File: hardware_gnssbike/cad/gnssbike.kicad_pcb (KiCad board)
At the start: 4 copper layers, 50 x 86 mm, 113 parts, among them J101 Molex 2036150003, J102 JST SM06B-GHS-TB, J201 Tag-Connect TC2030-NL, J401 Hirose FH28-10S-0.5SH, J402 Molex 503480-0500, Q401 DMG1012T-7, Q601 DMG1012T-7, Q602 DMG1012T-7, Q603 DMG1012T-7, SW601 Omron B3S-1002P, SW602 Omron B3S-1002P, SW603 Omron B3S-1002P, U101 nPM1300-QEAA, U102 MAX17262REWL, U103 AEM10900, U104 TPS7A0218PDQN, U201 MinewSemi ME54BS13, U301 u-blox MAX-F10S, U302 TI TXU0204BQAR, U501 MX25R6435F, U502 Bosch BMP585, U503 Bosch BMI270, U504 MMC5633NJL, U505 TI OPT3001DNPR

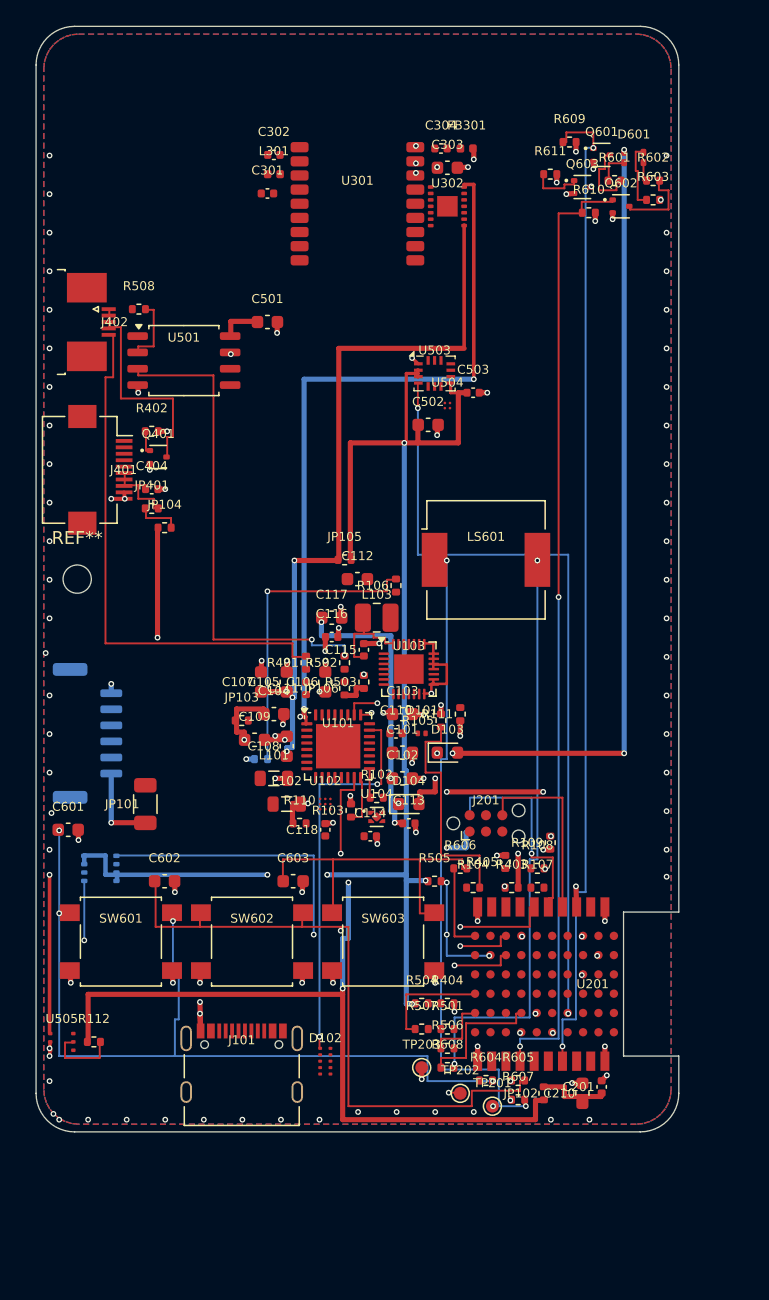
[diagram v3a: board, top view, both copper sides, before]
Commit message: fix(hardware): 45 degree corners, a 50 ohm line, and the stack-up that allows it
Three things the owner was right to call out, and one of them ran deeper than
it looked.

The router could only move four ways, so EVERY corner it drew was a right
angle. It now moves eight, with the guard that a diagonal step may not cut a
corner: both orthogonal cells it passes between have to be free too. Of 755
segments, 331 are now diagonal.

The RF line was left unrouted with the excuse that the 50 ohm width "does not
exist yet". It does: the stack-up is in the board file. Solving Hammerstad's
microstrip formula for 50 ohm on the dielectric that was there, 0.22 mm, gives
0.431 mm of track - and that is why the excuse held, because 0.431 mm cannot
leave the receiver's pin between pads on a 1.1 mm pitch.

The answer was not to give up but to read the sentence after the requirement.
Section 4.4 of the MAX-F10S integration manual says to "select the stack-up,
copper, and dielectric properties of the PCB accordingly to fulfil this
condition". The stack-up serves the RF line, not the other way round. It is
now asymmetric - 0.10 mm of prepreg to the ground plane, a 0.46 mm core,
0.10 mm back - which is the usual four layer arrangement for a board with RF
and brings 50 ohm to 0.196 mm. RF_ANT routes at that width.

And the rule this file had added itself - no signal under the GNSS receiver,
from the same section 4.4 - was blocking the receiver's own RF line, which
lives under the receiver by definition. "Signal lines crossing below" means
somebody else's. The RF nets now route first and the area closes behind them.

Five manufacturer datasheets were read for their layout sections, and two of
their rules are measurable and are now measured:

  TPS7A02 SBVS277C 8.4.1: no thermal via directly beneath the thermal pad of
  a DQN package - it wicks solder away from the joint;
  OPT3001: no component closer than twice its own height to the light
  sensor, because of secondary optical reflections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
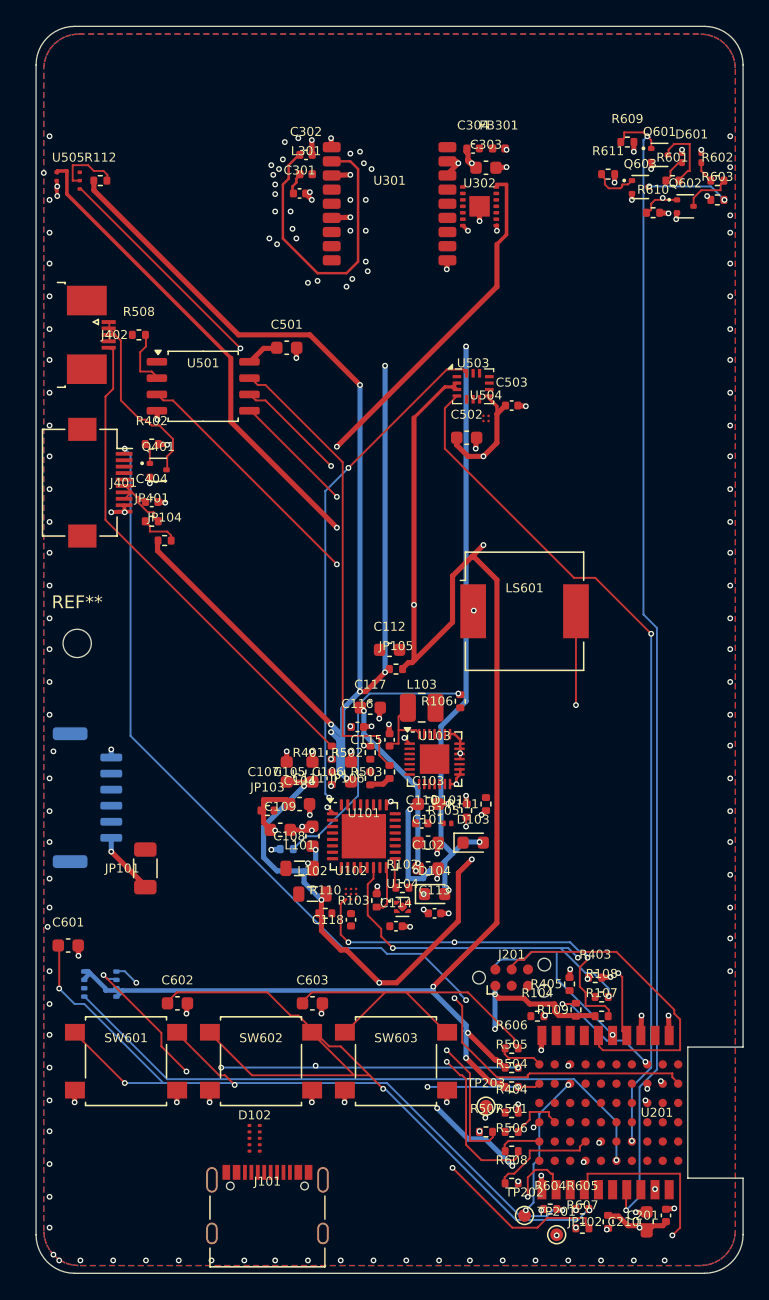
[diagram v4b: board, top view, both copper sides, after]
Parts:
- moved R112 67.0 mm to (30.0, 37.0)
- moved U505 67.0 mm to (27.5, 37.0)
- moved R505 15.7 mm to (62.0, 106.0)
- moved R606 14.6 mm to (62.0, 104.5)
- moved R109 13.2 mm to (67.0, 101.5)
- moved J201 12.2 mm to (62.0, 99.0)
- moved C201 11.2 mm to (74.0, 117.5)
- moved C210 11.2 mm to (72.5, 118.0)
- moved JP102 11.2 mm to (69.5, 118.0)
- moved R104 11.2 mm to (64.0, 102.0)
- moved R107 11.2 mm to (69.0, 102.0)
- moved R108 11.2 mm to (69.0, 100.5)
- moved R604 11.2 mm to (65.0, 117.0)
- moved R605 11.2 mm to (67.5, 117.0)
- moved R607 11.2 mm to (67.5, 118.5)
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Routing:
- net SENS_SDA: track 0.00 -> 101.1 mm, vias 0 -> 6
- net DISP_SCK: track 0.00 -> 77.4 mm, vias 0 -> 3
- net GNSS_RESET_N: track 71.4 -> 0.00 mm, vias 2 -> 0
- net NOR_SCK_F: track 0.00 -> 71.0 mm, vias 0 -> 2
- net SENS_SCL: track 41.8 -> 110.3 mm, vias 4 -> 5
- net NOR_MOSI_F: track 0.00 -> 67.9 mm, vias 0 -> 2
- net PWR_SDA: track 0.00 -> 56.3 mm, vias 0 -> 4
- net 3V0_SENS: track 134.9 -> 178.5 mm, vias 6 -> 7
- net 3V0: track 203.8 -> 242.1 mm, vias 14 -> 20
- net CC1: track 30.5 -> 0.00 mm, vias 2 -> 0
- net PWR_SCL: track 11.1 -> 40.8 mm, vias 2 -> 4
- net RF_IN: track 0.00 -> 24.0 mm
- net RGB_G: track 74.2 -> 97.7 mm
- net RGB_R: track 77.8 -> 90.6 mm
- net LED_CHG: track 11.2 -> 0.00 mm, vias 2 -> 0
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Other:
- board size 50 x 86 mm -> 55 x 97 mm

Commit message: feat(hardware): the AEM10900's own layout rules, and two real heights
The energy harvester's datasheet has a layout section and this board was not
following it. Section 13 of DS-AEM1090x-v2.4.0, word for word: "PCB track
capacitance must be reduced as much as possible on the boost converter
switching node SWDCDC. This is done as follows: keep the connection between
the SWDCDC pin and the inductor short; REMOVE THE GROUND AND POWER PLANES
UNDER THE SWDCDC NODE - the polygon on the opposite external layer may also
be removed - increase the distance between SWDCDC and the ground polygon on
the external PCB layer where the AEM1090x is mounted." And the same for
TH_REF.

Every pour on this board covered that node. A plane under a switching node is
capacitance the converter charges and discharges at its switching frequency,
and on a harvester that runs on microwatts that is not a detail. The board
now carries a computed keep-out over each of the two nodes - computed,
because it follows wherever the placer puts the part - and it forbids the
POUR, not the track: the node's own copper has to be there, and forbidding it
too put sixteen items_not_allowed in the DRC, every one of them the switching
node itself. The router also keeps its stitching vias out, since a ground via
there brings the plane straight back.

Two heights stopped being guesses. The tactile key is 3.4 mm, not the 5.0 mm
this file assumed, read off the dimensioned drawing on page 2 of the Omron
B3S datasheet - body 6.0 x 6.0, plunger 3.3 mm across standing 0.7 mm proud.
The buzzer is 11.0 x 9.0 x 1.7 mm, from the CPT-1117-83-SMT datasheet, which
is the part on the bill of materials; the 3.0 mm here was for the CPT-9019S
that only the footprint is named after.

Ten more manufacturer datasheets came in from the earlier work in this
session and now sit in datasheets/, which the .gitignore keeps out of this
public repository: the AEM10900, the Omron key, the buzzer, the USB-C
receptacle, the FPC connector, the fla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
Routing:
- net GND: track 52.5 -> 51.9 mm, vias 176 -> 174
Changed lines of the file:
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@@
 	)
 	(zone
+		(net 0)
+		(net_name "")
+		(layers "F.Cu" "In1.Cu" "In2.Cu" "B.Cu")
+		(name "SEM_PLANO_SW_DCDC")
+		(hatch edge 0.5)
+		(connect_pads
+			(clearance 0)
+		)
+		(min_thickness 0.25)
+		(filled_areas_thickness no)
+		(keepout
+			(tracks allowed)
+(pads allowed)
+			(copperpour not_allowed)
+			(footprints allowed)
+		)
+		(fill
+			(thermal_gap 0.5)
+			(thermal_bridge_width 0.5)
+		)
+		(polygon
+			(pts
+				(xy 53.4625 77.4000)
+				(xy 56.6750 77.4000)
+				(xy 56.6750 83.0000)
+				(xy 53.4625 83.0000)
+			)
+		)
+	)
+	(zone
+		(net 0)
+		(net_name "")
+		(layers "F.Cu" "In1.Cu" "In2.Cu" "B.Cu")
+		(name "SEM_PLANO_TH_REF")
+		(hatch edge 0.5)
+		(connect_pads
+			(clearance 0)
+		)
+		(min_thickness 0.25)
+		(filled_areas_thickness no)
+		(keepout
+			(tracks allowed)
+(pads allowed)
+			(copperpour not_allowed)
+			(footprints allowed)
+		)
+		(fill
+			(thermal_gap 0.5)
+			(thermal_bridge_width 0.5)
+		)
+		(polygon
+			(pts
+				(xy 55.2000 77.6100)
+				(xy 58.4000 77.6100)
+				(xy 58.4000 80.4625)
+				(xy 55.2000 80.4625)
+			)
+		)
+	)
+	(zone
 		(net 32)
 		(net_name "GND")
@@
 	)
 	(segment
-		(start 54.0625 80.8000)
-		(end 53.6500 80.3500)
-		(width 0.2)
-		(layer "F.Cu")
-		(net 32)
-	)
-	(segment
 		(start 74.2500 103.5000)
 		(end 74.2000 101.9500)
@@
 	)
 	(segment
+		(start 45.5500 36.5500)
+		(end 44.9500 37.1500)
+		(width 0.196)
+		(layer "F.Cu")
+		(net 68)
+	)
+	(segment
+		(start 44.9500 37.1500)
+		(end 44.9500 38.0500)
+		(width 0.196)
+		(layer "F.Cu")
+		(net 68)
+	)
+	(segment
 		(start 47.9500 35.5000)
 		(end 49.4500 35.5000)
@@
 	(segment
 		(start 44.2000 41.5000)
-		(end 44.2000 37.3000)
+		(end 44.2000 37.1500)
 		(width 0.196)
 		(layer "F.Cu")
@@
 	)
 	(segment
-		(start 44.2000 37.3000)
-		(end 44.6500 36.8500)
+		(start 44.2000 37.1500)
+		(end 44.6500 36.7000)
 		(width 0.196)
 		(layer "F.Cu")
@@
 	)
 	(segment
-		(start 44.6500 36.8500)
+		(start 44.6500 36.7000)
 		(end 44.6500 35.8000)
 		(width 0.196)
@@
 	)
 	(segment
-		(start 45.5500 36.5500)
-		(end 45.2500 36.8500)
-		(width 0.196)
-		(layer "F.Cu")
-		(net 68)
-	)
-	(segment
-		(start 45.2500 36.8500)
-		(end 45.2500 37.1500)
-		(width 0.196)
-		(layer "F.Cu")
-		(net 68)
-	)
-	(segment
-		(start 45.2500 37.1500)
-		(end 44.9500 37.4500)
-		(width 0.196)
-		(layer "F.Cu")
-		(net 68)
-	)
-	(segment
-		(start 44.9500 37.4500)
-		(end 44.9500 38.0500)
-		(width 0.196)
-		(layer "F.Cu")
-		(net 68)
-	)
-	(segment
 		(start 28.4500 37.0000)
 		(end 27.8500 37.0000)
@@
 	(segment
 		(start 57.7000 83.9500)
-		(end 54.7000 80.9500)
-		(width 0.2)
-		(layer "In2.Cu")
-		(net 99)
-	)
-	(segment
-		(start 54.7000 80.9500)
-		(end 52.6000 80.9500)
+		(end 53.8000 80.0500)
 		(width 0.2)
 		(layer "In2.Cu")
@@
 	)
 	(segment
-		(start 52.6000 80.9500)
-		(end 51.7000 80.0500)
-		(width 0.4)
-		(layer "In2.Cu")
-		(net 99)
-	)
-	(segment
-		(start 51.7000 80.0500)
+		(start 53.8000 80.0500)
 		(end 50.5000 80.0500)
 		(width 0.4)
@@
 	)
 	(via
-		(at 53.6500 80.3500)
-		(size 0.45)
-		(drill 0.25)
-		(layers "F.Cu" "B.Cu")
-		(net 32)
-	)
-	(via
 		(at 74.2000 101.9500)
 		(size 0.45)
@@
 	)
 	(via
+		(at 43.9000 36.1000)
+		(size 0.45)
+		(drill 0.25)
+		(layers "F.Cu" "B.Cu")
+		(net 32)
+	)
+	(via
+		(at 43.6000 37.1500)
+		(size 0.45)
+		(drill 0.25)
+		(layers "F.Cu" "B.Cu")
+		(net 32)
+	)
+	(via
+		(at 43.6000 38.0500)
+		(size 0.45)
+		(drill 0.25)
+		(layers "F.Cu" "B.Cu")
+		(net 32)
+	)
+	(via
 		(at 49.4500 34.9000)
 		(size 0.45)
@@
 	)
 	(via
-		(at 43.6000 37.3000)
+		(at 42.8500 37.1500)
 		(size 0.45)
 		(drill 0.25)
@@
 	)
 	(via
-		(at 43.4500 36.5500)
-		(size 0.45)
-		(drill 0.25)
-		(layers "F.Cu" "B.Cu")
-		(net 32)
-	)
-	(via
-		(at 43.9000 36.1000)
-		(size 0.45)
-		(drill 0.25)
-		(layers "F.Cu" "B.Cu")
-		(net 32)
-	)
-	(via
-		(at 43.3000 35.8000)
+		(at 43.1500 36.1000)
 		(size 0.45)
 		(drill 0.25)
@@
 		(size 0.45)
 		(drill 0.25)
-		(layers "F.Cu" "B.Cu")
-		(net 32)
-	)
-	(via
-		(at 46.3000 37.9000)
-		(size 0.45)
-		(drill 0.25)
-		(layers "F.Cu" "B.Cu")
-		(net 32)
-	)
-	(via
-		(at 43.6000 38.0500)
-		(size 0.45)
-		(drill 0.25)

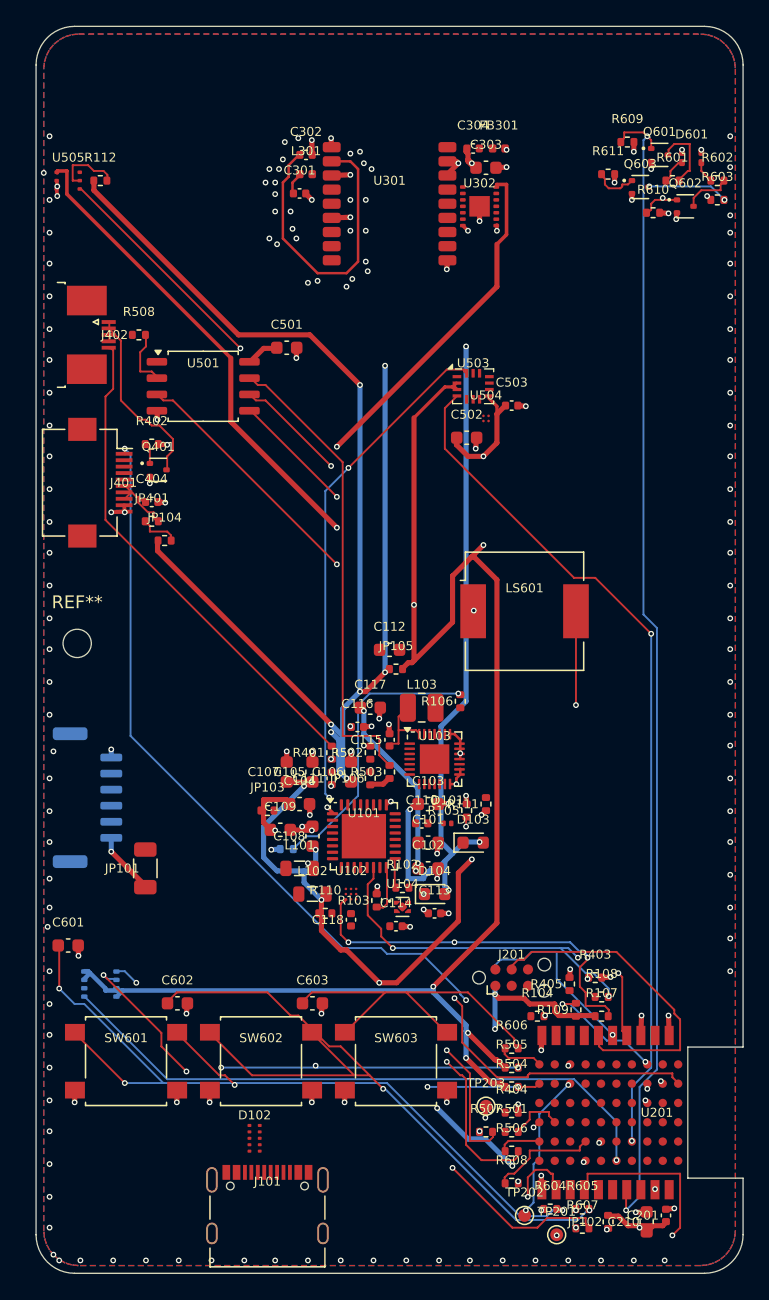
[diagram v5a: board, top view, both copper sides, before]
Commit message: fix(hardware): the solar panel and the antenna had nowhere to touch the board
This board could not be built. The six solar modules live in the case and
connect to SRC and GND; the GNSS antenna element lives in the case wall and
connects to RF_ANT and GND. On the board, SRC reached only the harvester, its
capacitor and its inductor, and RF_ANT reached only the pi network. There was
no pad for either of them. The wires had nowhere to land.

04-pcb-e-caixa.md had already decided how they arrive - the antenna "com
contatos de mola" on line 271, the panels "em 3 grupos, mola ou FPC" on line
388 - and line 661 listed as open that "a area dos pads de mola e dos
conectores dos tres grupos de paineis nao esta dimensionada em lugar nenhum".
It is dimensioned now: two 2.0 x 2.0 mm gold pads at 3.0 mm pitch, with no
paste, because a spring presses on them and nothing is soldered.

J302 takes the antenna, just below its keep-out and a few millimetres from
the pi network, which is what the same document asks for when it says the
50 ohm line is "poucos mm". J103, J104 and J105 take the three groups of
panels, in the free bands of the two edges - computed, not guessed: the left
edge is taken by the light sensor, the two flat cables, the M2 hole, the
battery connector and a key. All three sit within about 15 mm of the
harvester, because SRC comes off a solar cell at high impedance and a long
run of it picks up everything.

The bodies stopped being identical black cuboids. What distinguishes these
packages at a glance is where the metal is, so a QFN now shows its exposed
pad and the ring of lead flags underneath, a SOIC stands on gull-wing leads
that reach out on two sides, a SOT has its three, and a wafer-level package
is bare silicon over a grid of balls. Each one carries the pin 1 dot. Every
dimension comes from the outline the footprint already had; what is new is
only which part of it is drawn as metal.

116 parts, no DRC error, 131 connections routed, and twelve of the thirteen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
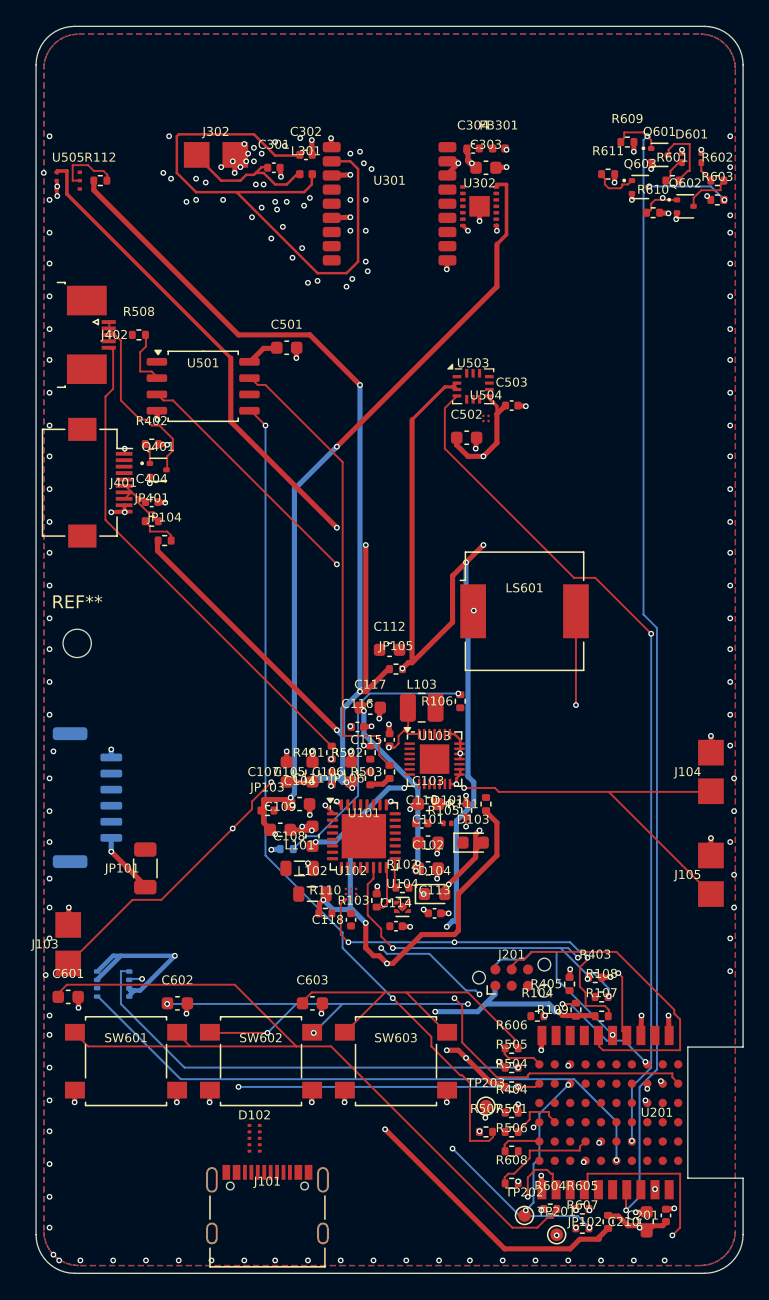
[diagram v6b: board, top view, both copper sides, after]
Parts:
- added J103: contato de mola, 2 vias, gnssbike:ContatoMola_2x2mm_P3mm, F.Cu at (27.5, 96.4)
- added J104: contato de mola, 2 vias, gnssbike:ContatoMola_2x2mm_P3mm, F.Cu at (77.5, 83.0)
- added J105: contato de mola, 2 vias, gnssbike:ContatoMola_2x2mm_P3mm, F.Cu at (77.5, 91.0)
- added J302: contato de mola, 2 vias, gnssbike:ContatoMola_2x2mm_P3mm, F.Cu at (39.0, 35.0)
- moved C601 4.00 mm to (27.5, 100.5)
- moved C301 2.83 mm to (43.5, 36.0)
- moved U502 1.00 mm to (31.0, 99.5)
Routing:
- net SRC: track 5.75 -> 87.8 mm, vias 0 -> 4
- net SENS_SCL: track 110.3 -> 36.1 mm, vias 5 -> 1
- net NOR_SCK_F: track 71.0 -> 0.00 mm, vias 2 -> 0
- net SENS_SDA: track 101.1 -> 36.1 mm, vias 6 -> 3
- net RF_IN: track 24.0 -> 47.3 mm
- net RF_ANT: track 1.75 -> 10.9 mm
- net 3V0: track 242.1 -> 233.8 mm, vias 20 -> 17
- net 3V0_SENS: track 178.5 -> 186.6 mm, vias 7 -> 10
- net GND: track 51.9 -> 57.3 mm, vias 174 -> 197
- net VSYS: track 80.3 -> 75.3 mm, vias 5 -> 4
- net 1V8: track 71.8 -> 69.2 mm, vias 4 -> 6
- net KEY_C_SW: track 59.6 -> 57.8 mm, vias 2 -> 5
- net BUZ_A_LS: track 57.7 -> 56.0 mm, vias 2 -> 3
- net KEY_L_SW: track 65.4 -> 67.1 mm, vias 4 -> 0
- net NOR_MOSI_F: track 67.9 -> 66.4 mm
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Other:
- board text added: "116 pecas colocadas, 8 fora da placa (painel, antena e modulos solares vivem na caixa)"
- board text removed: "112 pecas colocadas, 8 fora da placa (painel, antena e modulos solares vivem na caixa)"
